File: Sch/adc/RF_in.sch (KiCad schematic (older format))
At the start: 67 parts, among them CN1 SMA, CN2 SMA, J3 JP2, J4 JP2, J5 JP2, U1 LTC2292, U2 BGA2818, U3 TLV702, U4 BGA2818

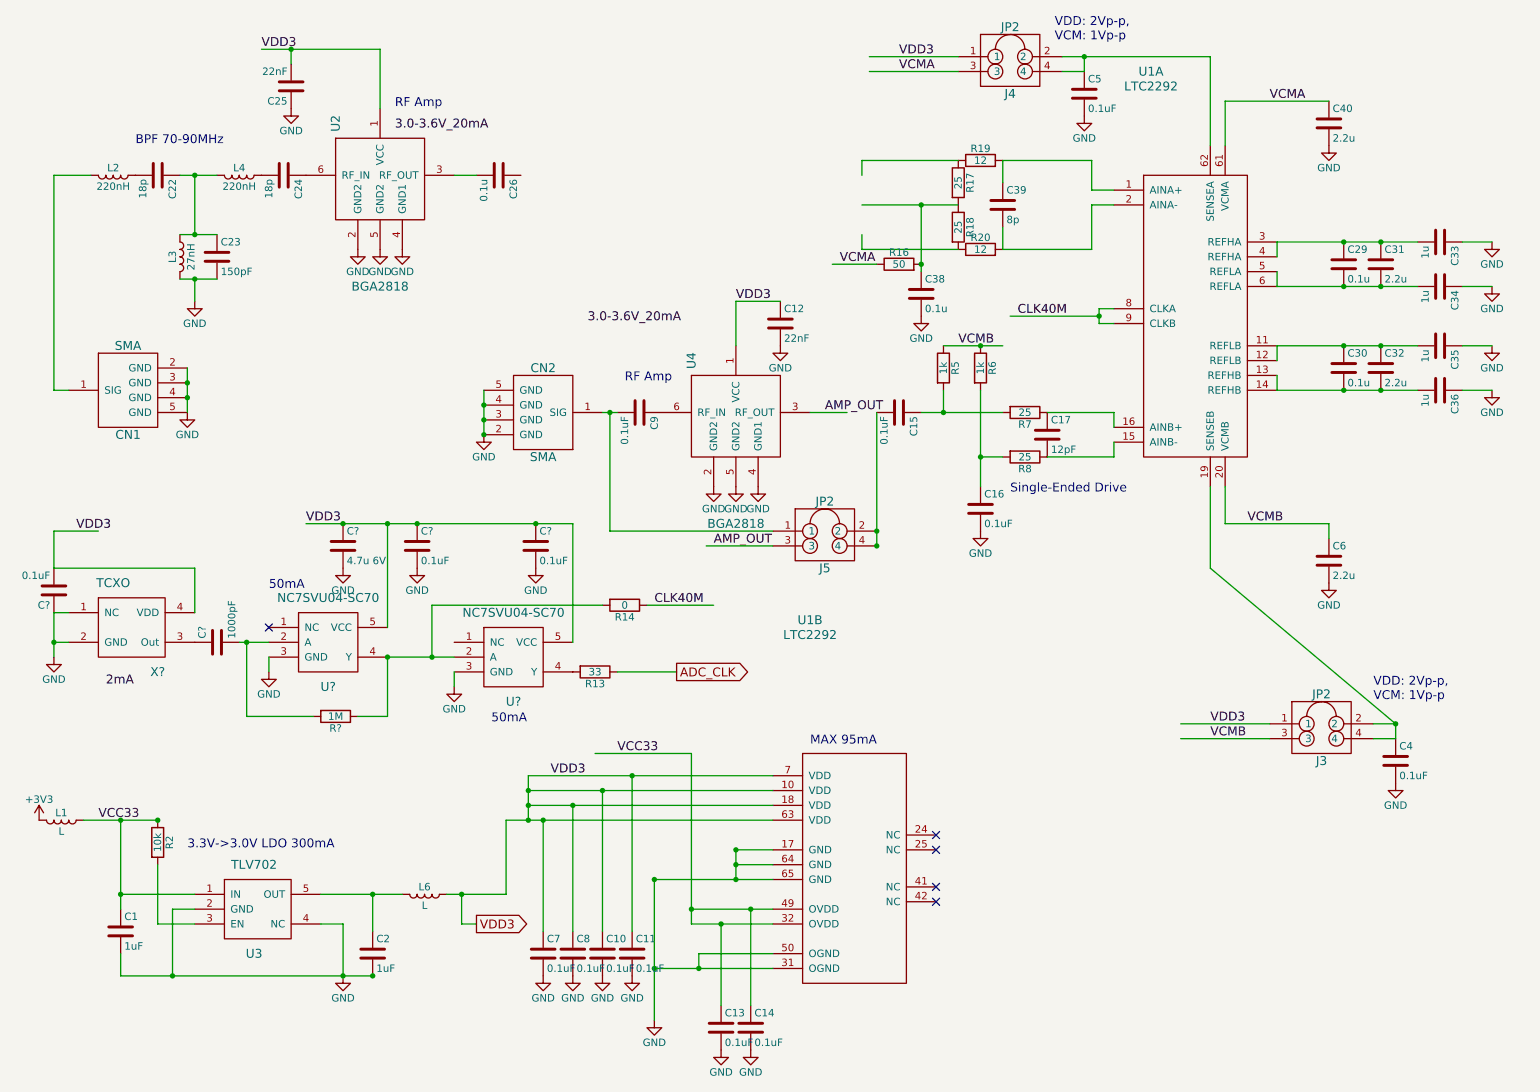
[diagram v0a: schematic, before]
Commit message: Changed transformer
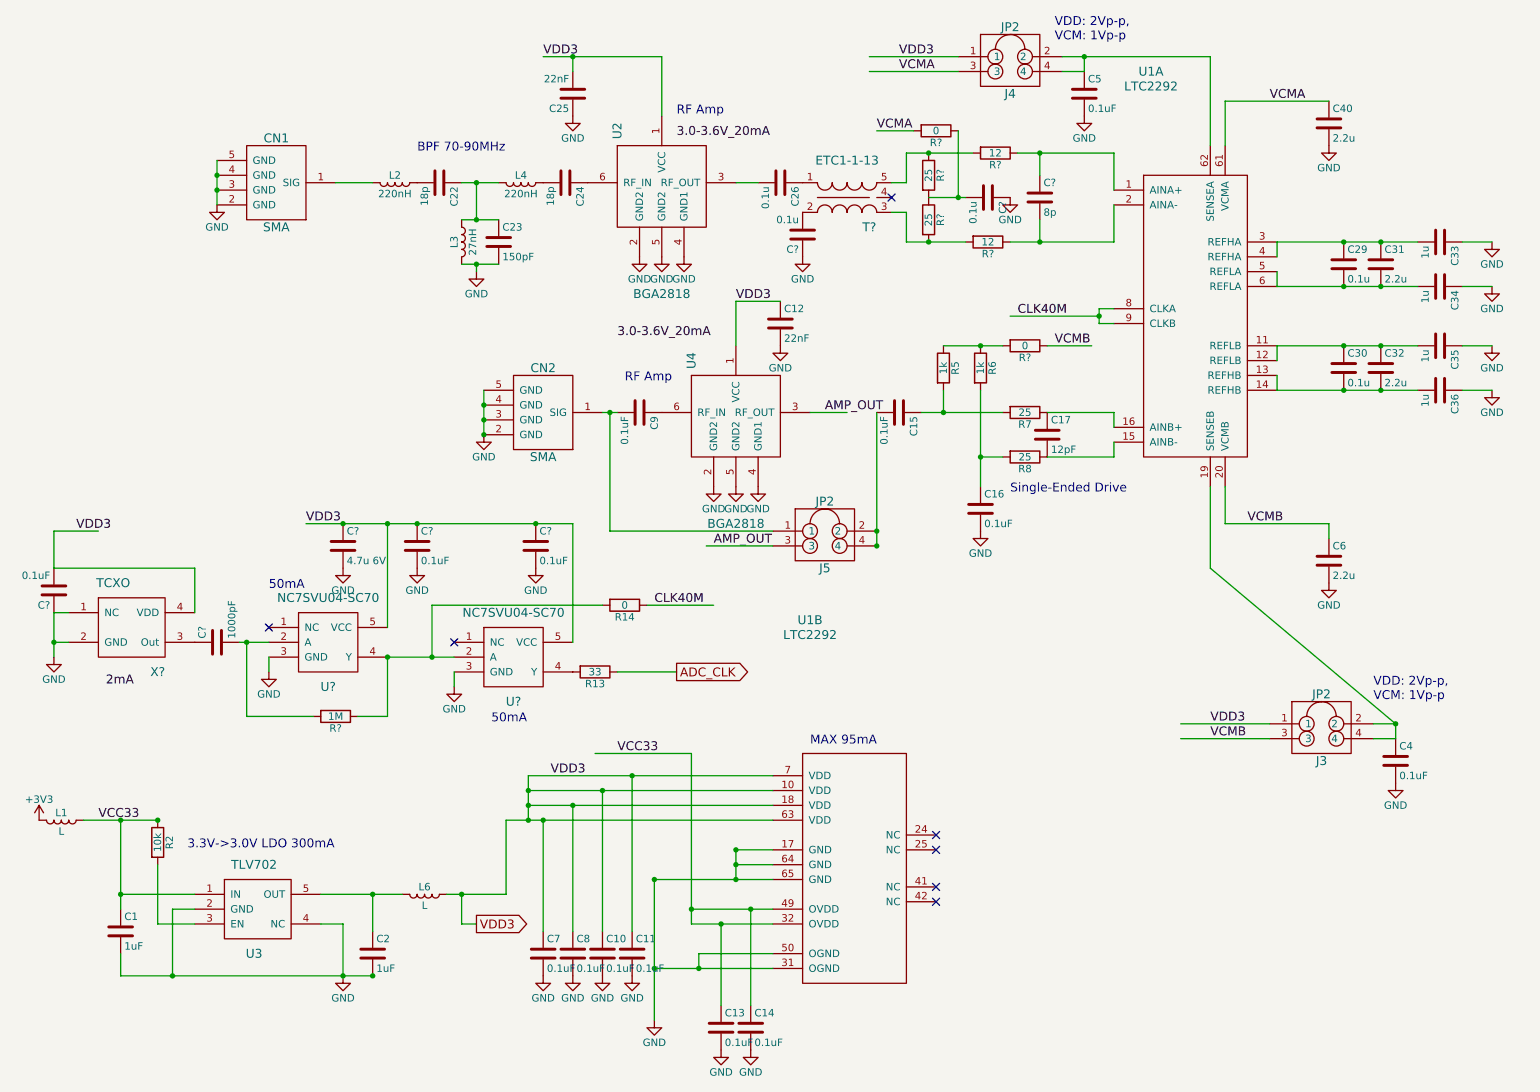
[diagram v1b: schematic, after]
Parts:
- removed C38: 0.1u, adc_lib:C0603, symbol C
- removed C39: 8p, adc_lib:C0603, symbol C
- removed R16: 50, adc_lib:R0603, symbol R
- removed R17, R18: 25, adc_lib:R0603, symbol R
- removed R19, R20: 12, adc_lib:R0603, symbol R
- added C? (x2): 0.1u, adc_lib:C0603, symbol C
- added C?: 8p, symbol C
- added R? (x2): 25, symbol R
- added R? (x2): 12, symbol R
- added R? (x2): 0, symbol R
- added T?: ETC1-1-13, symbol ETC1-1-13
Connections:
- wire segments 194 -> 141
- no-connect marks 5 -> 7
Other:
- moved on the sheet: C22, C23, C24, C25, C26, CN1, L2, L3, L4, U2

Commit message: Changed PDS
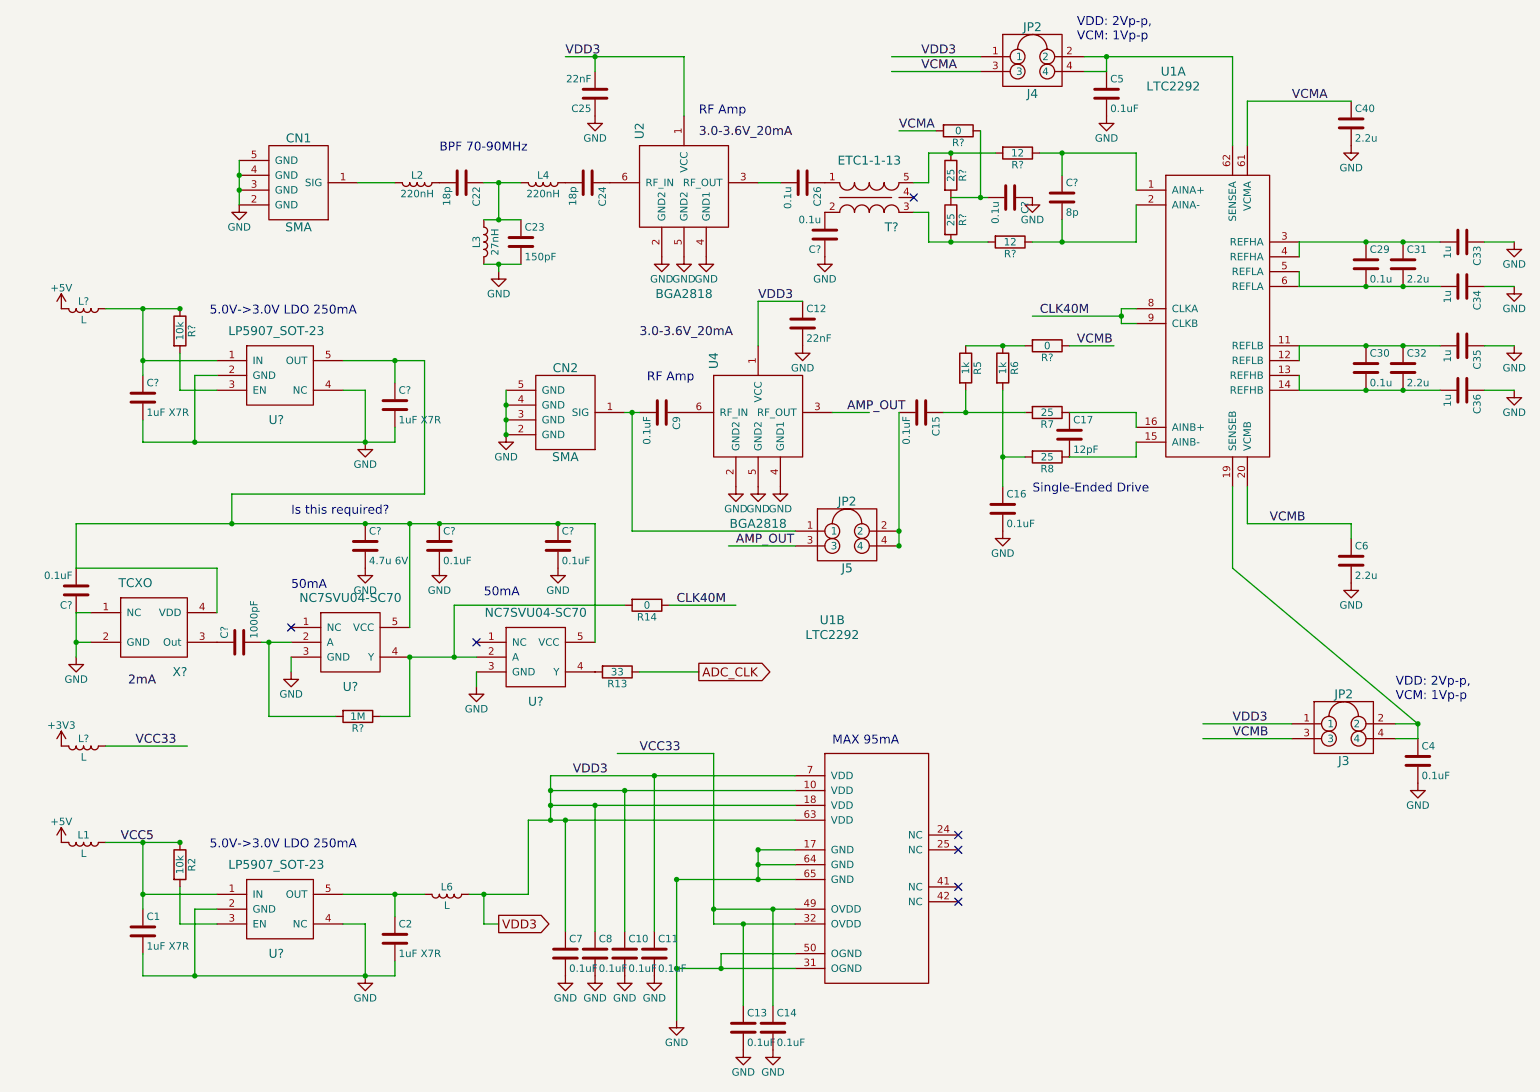
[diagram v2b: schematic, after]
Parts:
- removed U3: TLV702, adc_lib:TLV702, symbol TLV702
- added C? (x2): 1uF X7R, adc_lib:C0603, symbol C
- added L? (x2): L, adc_lib:FB0805, symbol L
- added R?: 10k, adc_lib:R0603, symbol R
- added U? (x2): LP5907_SOT-23, symbol LP5907_SOT-23
- C1, C2: value 1uF -> 1uF X7R
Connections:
- net labels added: +5V, VCC5
- wire segments 141 -> 159
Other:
- note added: "5.0V->3.0V LDO 250mA"
- note added: "Is this required?"
- note removed: "3.3V->3.0V LDO 300mA"
- moved on the sheet: C1, C10, C11, C12, C13, C14, C15, C16, C17, C2, C22, C23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

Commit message: Add pull-down to BP net. Remove RF amp of 2nd input to the ADC.
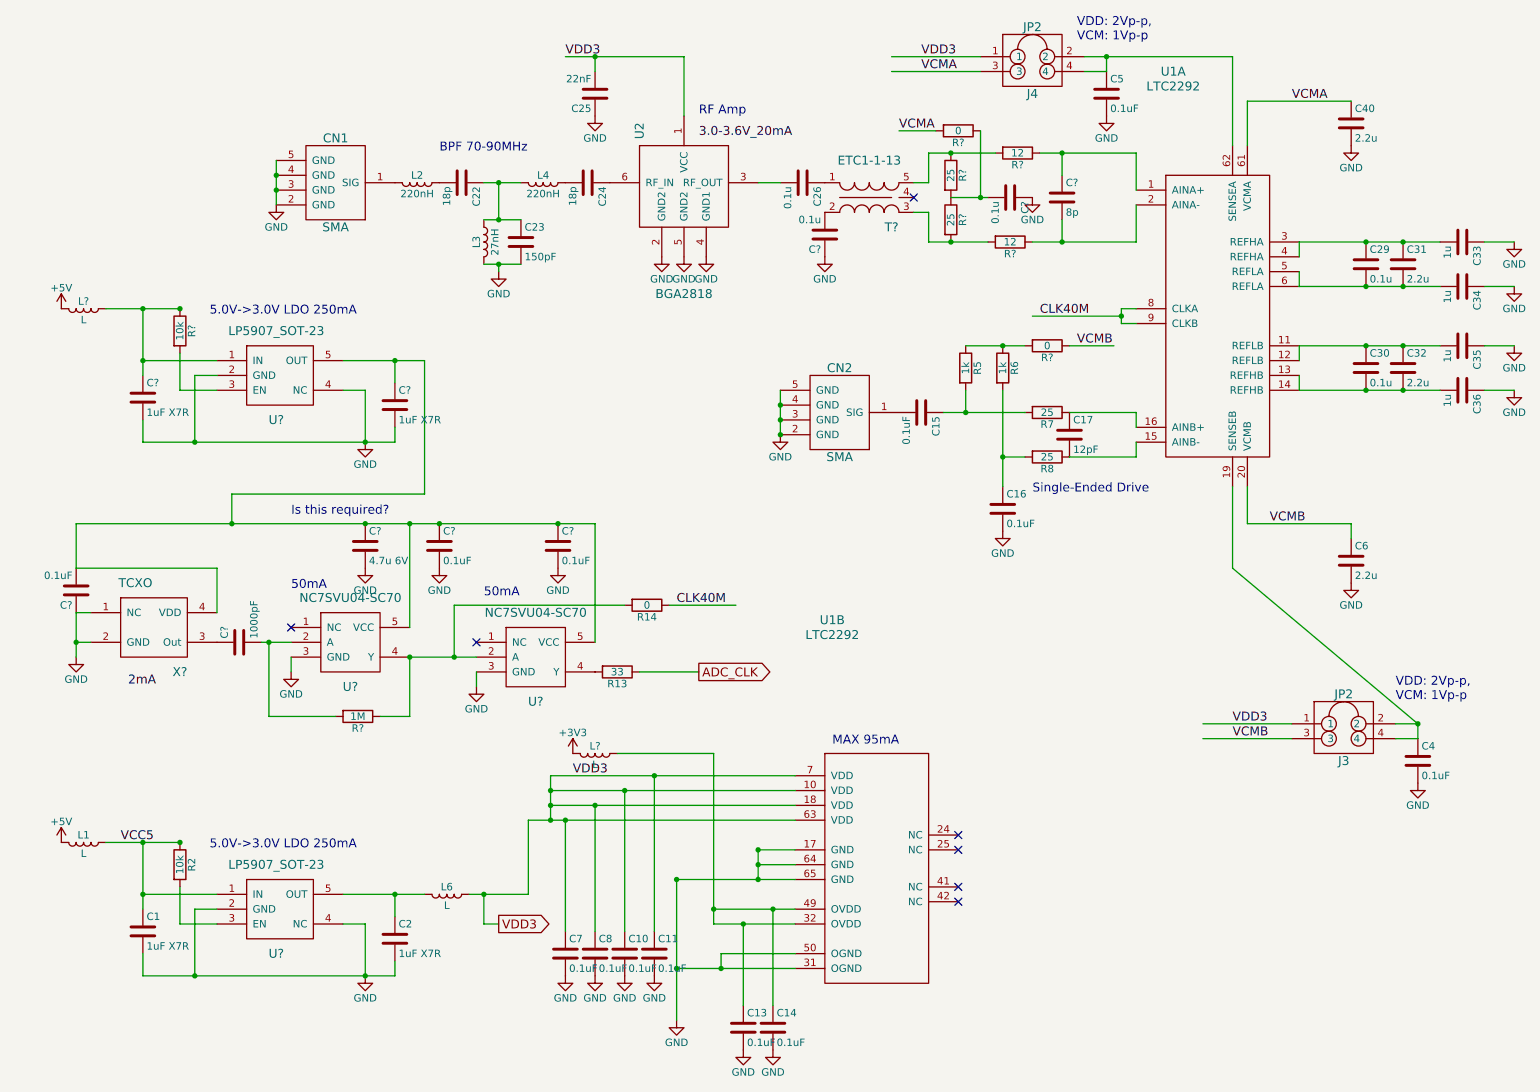
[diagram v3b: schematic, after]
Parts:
- removed C12: 22nF, adc_lib:C0603, symbol C
- removed C9: 0.1uF, adc_lib:C0603, symbol C
- removed J5: JP2, adc_lib:M20-9980245, symbol JP2
- removed U4: BGA2818, adc_lib:BGA2818, symbol BGA2818
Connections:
- net labels removed: AMP_OUT, VCC33
- wire segments 159 -> 149
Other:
- moved on the sheet: CN1, CN2, L?
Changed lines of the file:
@@
 L SMA CN1
 U 1 1 58A7A7C8
-P 2400 1650
-F 0 "CN1" H 2400 1350 60  0000 C CNN
-F 1 "SMA" H 2400 1950 60  0000 C CNN
-F 2 "adc_lib:SMA_RightAngle" H 2300 1650 60  0001 C CNN
-F 3 "" H 2300 1650 60  0001 C CNN
-	1    2400 1650
+P 2650 1650
+F 0 "CN1" H 2650 1350 60  0000 C CNN
+F 1 "SMA" H 2650 1950 60  0000 C CNN
+F 2 "adc_lib:SMA_RightAngle" H 2550 1650 60  0001 C CNN
+F 3 "" H 2550 1650 60  0001 C CNN
+	1    2650 1650
 	-1   0    0    1
 $EndComp
@@
 L SMA CN2
 U 1 1 58A7B9DB
-P 4200 3200
-F 0 "CN2" H 4200 2900 60  0000 C CNN
-F 1 "SMA" H 4200 3500 60  0000 C CNN
-F 2 "adc_lib:SMA_RightAngle" H 4100 3200 60  0001 C CNN
-F 3 "" H 4100 3200 60  0001 C CNN
-	1    4200 3200
+P 6050 3200
+F 0 "CN2" H 6050 2900 60  0000 C CNN
+F 1 "SMA" H 6050 3500 60  0000 C CNN
+F 2 "adc_lib:SMA_RightAngle" H 5950 3200 60  0001 C CNN
+F 3 "" H 5950 3200 60  0001 C CNN
+	1    6050 3200
 	-1   0    0    1
 $EndComp
-$Comp
-L GND #PWR043
-U 1 1 58A7B9E1
-P 5350 3700
-F 0 "#PWR043" H 5350 3450 50  0001 C CNN
-F 1 "GND" H 5350 3550 50  0000 C CNN
-F 2 "" H 5350 3700 50  0000 C CNN
-F 3 "" H 5350 3700 50  0000 C CNN
-	1    5350 3700
-	1    0    0    -1
-$EndComp
-$Comp
-L BGA2818 U4
-U 1 1 58A8393B
-P 5500 3250
-F 0 "U4" V 5200 3650 60  0000 C CNN
-F 1 "BGA2818" H 5500 2550 60  0000 C CNN
-F 2 "adc_lib:BGA2818" H 5500 3300 60  0001 C CNN
-F 3 "" H 5500 3300 60  0001 C CNN
-	1    5500 3250
-	1    0    0    -1
-$EndComp
-$Comp
-L GND #PWR044
-U 1 1 58A83941
-P 5800 2750
-F 0 "#PWR044" H 5800 2500 50  0001 C CNN
-F 1 "GND" H 5800 2600 50  0000 C CNN
-F 2 "" H 5800 2750 50  0000 C CNN
-F 3 "" H 5800 2750 50  0000 C CNN
-	1    5800 2750
-	1    0    0    -1
-$EndComp
-$Comp
-L C C12
-U 1 1 58A8394D
-P 5800 2600
-F 0 "C12" H 5825 2700 50  0000 L CNN
-F 1 "22nF" H 5825 2500 50  0000 L CNN
-F 2 "adc_lib:C0603" H 5838 2450 50  0001 C CNN
-F 3 "" H 5800 2600 50  0000 C CNN
-	1    5800 2600
-	1    0    0    -1
-$EndComp
-Text Notes 4750 3000 0    60   ~ 0
-RF Amp
-$Comp
-L C C9
-U 1 1 58A84A99
-P 4850 3200
-F 0 "C9" H 4875 3300 50  0000 L CNN
-F 1 "0.1uF" H 4875 3100 50  0000 L CNN
-F 2 "adc_lib:C0603" H 4888 3050 50  0001 C CNN
-F 3 "" H 4850 3200 50  0000 C CNN
-	1    4850 3200
-	0    1    1    0
-$EndComp
-$Comp
-L JP2 J5
-U 1 1 58A84E76
-P 6100 4000
-F 0 "J5" H 6100 3750 60  0000 C CNN
-F 1 "JP2" H 6100 4200 60  0000 C CNN
-F 2 "adc_lib:M20-9980245" H 6050 4100 60  0001 C CNN
-F 3 "" H 6050 4100 60  0001 C CNN
-	1    6100 4000
-	1    0    0    -1
-$EndComp
-$Comp
-L GND #PWR045
-U 1 1 58A85320
-P 5500 3700
-F 0 "#PWR045" H 5500 3450 50  0001 C CNN
-F 1 "GND" H 5500 3550 50  0000 C CNN
-F 2 "" H 5500 3700 50  0000 C CNN
-F 3 "" H 5500 3700 50  0000 C CNN
-	1    5500 3700
-	1    0    0    -1
-$EndComp
-$Comp
-L GND #PWR046
-U 1 1 58A853F7
-P 5650 3700
-F 0 "#PWR046" H 5650 3450 50  0001 C CNN
-F 1 "GND" H 5650 3550 50  0000 C CNN
-F 2 "" H 5650 3700 50  0000 C CNN
-F 3 "" H 5650 3700 50  0000 C CNN
-	1    5650 3700
-	1    0    0    -1
-$EndComp
-Text Label 6100 3200 0    60   ~ 0
-AMP_OUT
-Text Label 5350 4100 0    60   ~ 0
-AMP_OUT
 Text Label 4950 4500 0    60   ~ 0
 CLK40M
@@
 L GND #PWR051
 U 1 1 58A8E85E
-P 3800 3350
-F 0 "#PWR051" H 3800 3100 50  0001 C CNN
-F 1 "GND" H 3800 3200 50  0000 C CNN
-F 2 "" H 3800 3350 50  0000 C CNN
-F 3 "" H 3800 3350 50  0000 C CNN
-	1    3800 3350
+P 5650 3350
+F 0 "#PWR051" H 5650 3100 50  0001 C CNN
+F 1 "GND" H 5650 3200 50  0000 C CNN
+F 2 "" H 5650 3350 50  0000 C CNN
+F 3 "" H 5650 3350 50  0000 C CNN
+	1    5650 3350
 	1    0    0    -1
 $EndComp
@@
 Text Label 1200 6100 0    60   ~ 0
 VCC5
-Text Label 4700 5500 0    60   ~ 0
-VCC33
 Text Label 4200 800  0    60   ~ 0
 VDD3
@@
 Text Notes 3650 4450 0    60   ~ 0
 50mA
-Text Label 4700 2700 0    60   ~ 0
-3.0-3.6V_20mA
-Text Label 5500 2450 0    60   ~ 0
-VDD3
 $Comp
 L C C?
@@
 Connection ~ 7150 3500
 Wire Wire Line
-	2000 1500 2000 1800
-Connection ~ 2000 1700
-Connection ~ 2000 1600
-Wire Wire Line
-	2800 1650 3050 1650
-Wire Wire Line
-	3800 3050 3800 3350
-Connection ~ 3800 3150
-Connection ~ 3800 3250
-Wire Wire Line
-	4600 3200 4700 3200
-Wire Wire Line
-	4650 4000 5750 4000
-Wire Wire Line
-	6450 3200 6450 4100
-Connection ~ 6450 4000
-Wire Wire Line
-	6000 3200 6250 3200
-Wire Wire Line
-	5750 4100 5300 4100
+	2250 1500 2250 1800
+Connection ~ 2250 1700
+Connection ~ 2250 1600
+Wire Wire Line
+	5650 3050 5650 3350
+Connection ~ 5650 3150
+Connection ~ 5650 3250
 Connection ~ 7150 2750
 Wire Wire Line
 	3450 4500 4600 4500
-Connection ~ 3800 3350
+Connection ~ 5650 3350
 Wire Wire Line
 	4700 4950 5100 4950
@@
 	1850 4550 1850 4250
 Wire Wire Line
-	900  4250 1850 4250
-Wire Wire Line
-	900  3950 900  4250
+	1850 4250 900  4250
+Wire Wire Line
+	900  4250 900  3950
 Wire Wire Line
 	2350 4850 2350 4950
@@
 Wire Wire Line
 	3600 4950 3600 5050
-Connection ~ 6450 4100
-Wire Wire Line
-	4650 3200 4650 4000
-Connection ~ 4650 3200
-Wire Wire Line
-	5800 2450 5500 2450
-Wire Wire Line
-	5500 2450 5500 2750
 Connection ~ 3350 3950
 Wire Wire Line
@@
 L GND #PWR?
 U 1 1 5956B4E5
-P 2000 1800
-F 0 "#PWR?" H 2000 1550 50  0001 C CNN
-F 1 "GND" H 2000 1650 50  0000 C CNN
-F 2 "" H 2000 1800 50  0000 C CNN
-F 3 "" H 2000 1800 50  0000 C CNN
-	1    2000 1800
+P 2250 1800
+F 0 "#PWR?" H 2250 1550 50  0001 C CNN
+F 1 "GND" H 2250 1650 50  0000 C CNN
+F 2 "" H 2250 1800 50  0000 C CNN
+F 3 "" H 2250 1800 50  0000 C CNN
+	1    2250 1800
 	1    0    0    -1
 $EndComp
@@
 L +3V3 #PWR?
 U 1 1 5956828F
-P 800 5450
-F 0 "#PWR?" H 800 5300 50  0001 C CNN
-F 1 "+3V3" H 800 5590 50  0000 C CNN
-F 2 "" H 800 5450 50  0000 C CNN
-F 3 "" H 800 5450 50  0000 C CNN
-	1    800  5450
+P 4250 5500
+F 0 "#PWR?" H 4250 5350 50  0001 C CNN
+F 1 "+3V3" H 4250 5640 50  0000 C CNN
+F 2 "" H 4250 5500 50  0000 C CNN
+F 3 "" H 4250 5500 50  0000 C CNN
+	1    4250 5500
 	1    0    0    -1
 $EndComp
@@
 L L L?
 U 1 1 595685CB
-P 950 5450
-F 0 "L?" V 900 5450 50  0000 C CNN
-F 1 "L" V 1025 5450 50  0000 C CNN
-F 2 "adc_lib:FB0805" H 950 5450 50  0001 C CNN
-F 3 "" H 950 5450 50  0000 C CNN
-	1    950  5450
-	0    1    1    0
-$EndComp
-Wire Wire Line
-	1100 5450 1650 5450
-Text Label 1300 5450 0    60   ~ 0
-VCC33
+P 4400 5500
+F 0 "L?" V 4350 5500 50  0000 C CNN
+F 1 "L" V 4475 5500 50  0000 C CNN
+F 2 "adc_lib:FB0805" H 4400 5500 50  0001 C CNN
+F 3 "" H 4400 5500 50  0000 C CNN
+	1    4400 5500
+	0    1    1    0
+$EndComp
 Wire Wire Line
 	3050 6450 3050 6600
